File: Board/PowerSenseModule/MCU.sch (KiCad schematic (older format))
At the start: 33 parts, among them J3 Programming Header, J4 Conn_01x02_Male, U2 NCV2007x, U3 dsPIC33EV32GM102, U4 MCP2542FDxMF

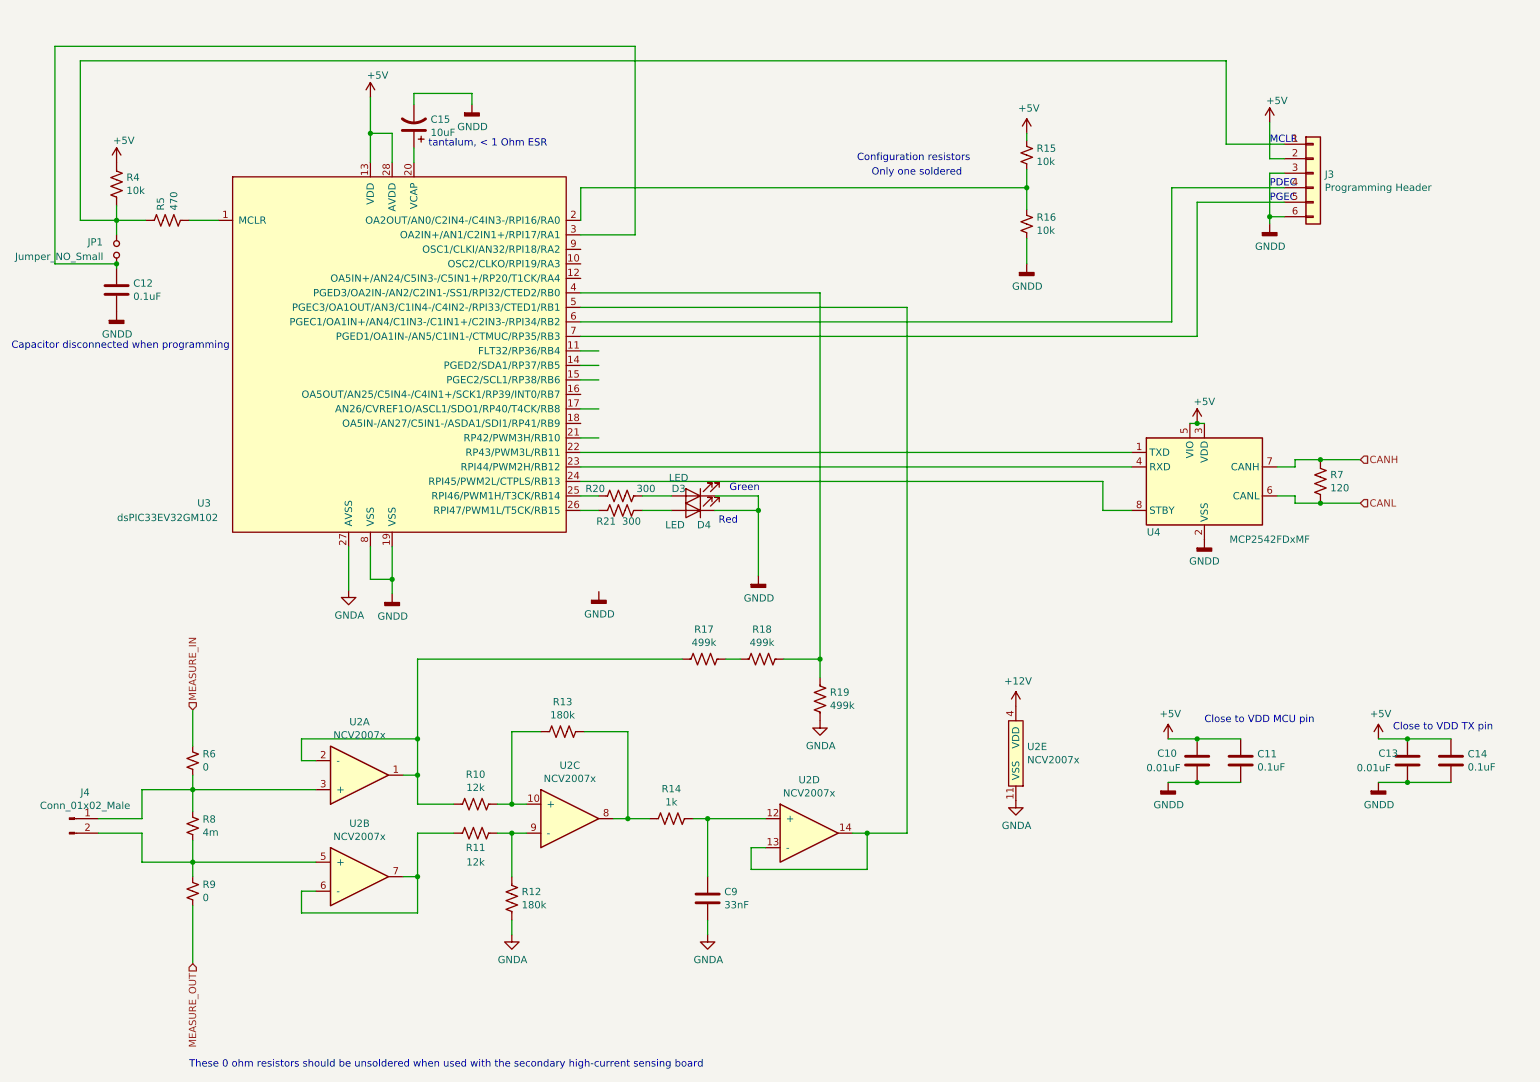
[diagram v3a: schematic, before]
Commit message: FINAL BASIS/REFERENCE
Rewiring done to proper pins on MCU
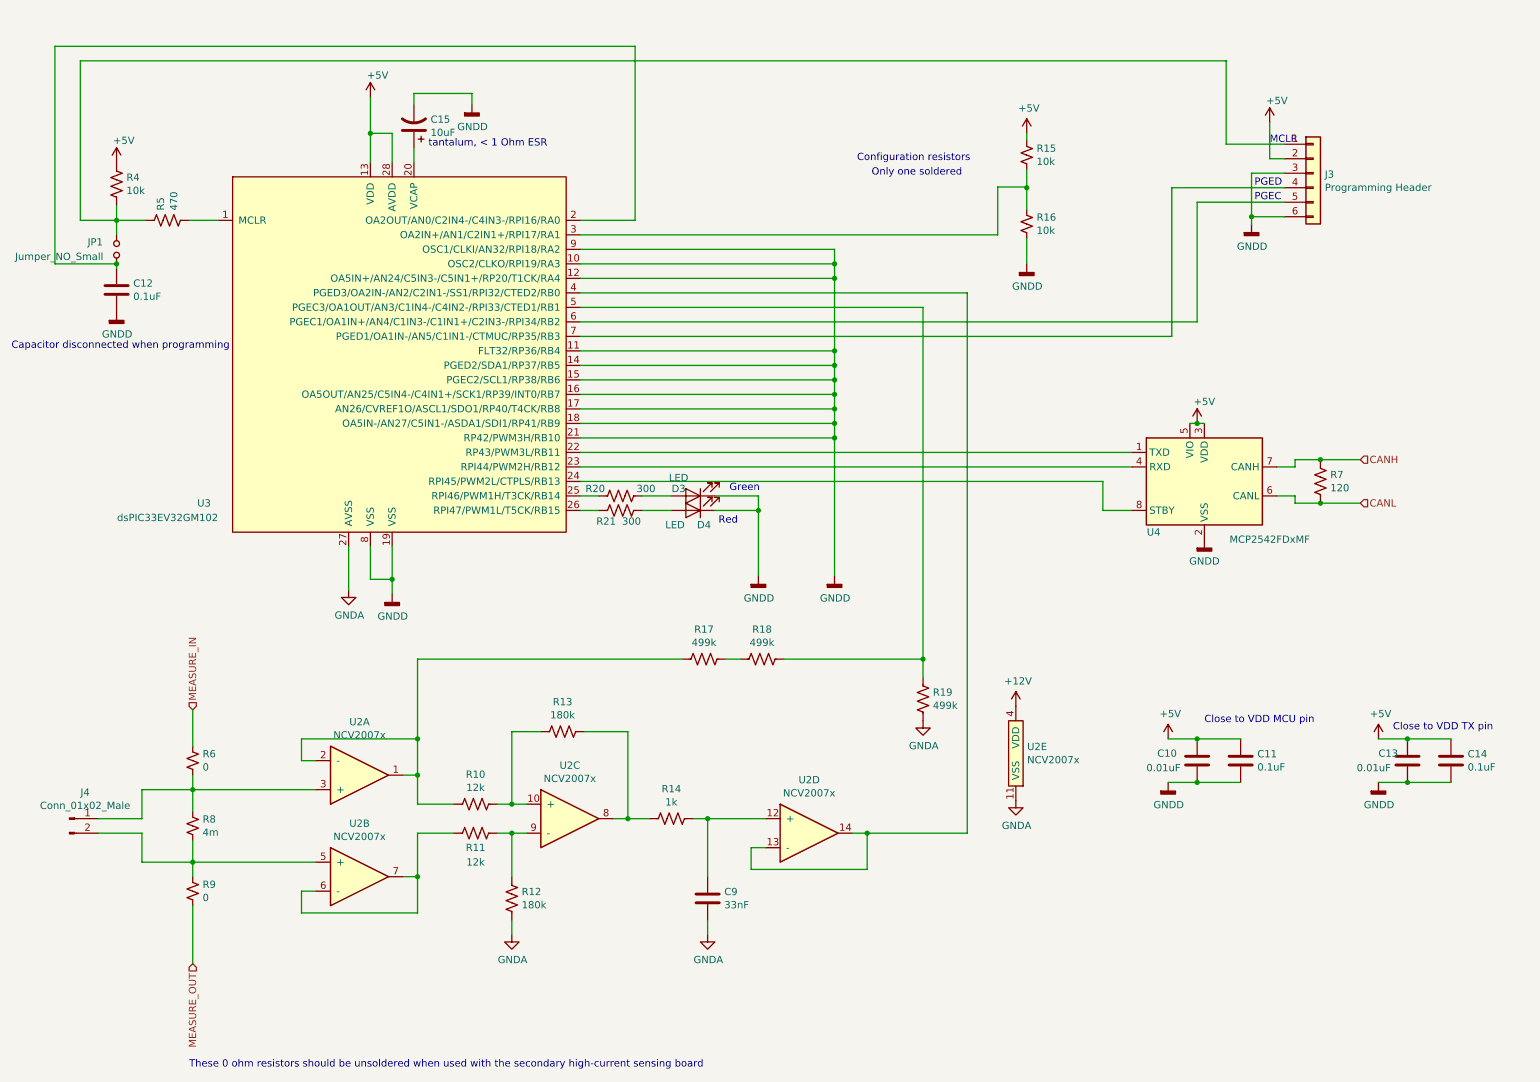
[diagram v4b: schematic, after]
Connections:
- wire segments 143 -> 159
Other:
- note added: "PGED\n"
- note removed: "PDEC"
- moved on the sheet: R19
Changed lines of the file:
@@
 	1925 1900 1725 1900
-$Comp
-L F1_Microchip_MCUs:dsPIC33EV32GM102 U3
-U 1 1 5D3ED3E3
-P 3175 5150
-F 0 "U3" H 1875 6450 50  0000 R CNN
-F 1 "dsPIC33EV32GM102" H 1925 6350 50  0000 R CNN
-F 2 "Package_SO:SSOP-28_5.3x10.2mm_P0.65mm" H 3175 5150 50  0001 C CNN
-F 3 "http://ww1.microchip.com/downloads/en/DeviceDoc/dsPIC33EVXXXGM00X-10X-Family-Data-Sheet-DS70005144H.pdf" H 3175 5150 50  0001 C CNN
-	1    3175 5150
-	1    0    0    -1
-$EndComp
 $Comp
 L Interface_CAN_LIN:MCP2542FDxMF U4
@@
 L power:GNDD #PWR028
 U 1 1 5D3C46D6
-P 9175 1925
-F 0 "#PWR028" H 9175 1675 50  0001 C CNN
-F 1 "GNDD" H 9179 1770 50  0000 C CNN
-F 2 "" H 9175 1925 50  0001 C CNN
-F 3 "" H 9175 1925 50  0001 C CNN
-	1    9175 1925
+P 9050 1925
+F 0 "#PWR028" H 9050 1675 50  0001 C CNN
+F 1 "GNDD" H 9054 1770 50  0000 C CNN
+F 2 "" H 9050 1925 50  0001 C CNN
+F 3 "" H 9050 1925 50  0001 C CNN
+	1    9050 1925
 	1    0    0    -1
 $EndComp
 Text Notes 9175 1375 0    50   ~ 0
 MCLR
-Text Notes 9175 1775 0    50   ~ 0
+Text Notes 9070 1770 0    50   ~ 0
 PGEC
-Text Notes 9175 1675 0    50   ~ 0
-PDEC
+Text Notes 9070 1670 0    50   ~ 0
+PGED\n
 Wire Wire Line
 	8875 1375 9275 1375
@@
 	975  1900 975  800
 Wire Wire Line
-	9175 1875 9175 1925
-Wire Wire Line
-	9275 1875 9175 1875
-Connection ~ 9175 1875
-Wire Wire Line
-	9175 1575 9175 1875
+	9050 1875 9050 1925
+Connection ~ 9050 1875
+Wire Wire Line
+	9050 1575 9050 1875
 Text HLabel 9800 3850 2    50   Input ~ 0
 CANL
@@
 Wire Wire Line
 	975  1900 1225 1900
-Wire Wire Line
-	9275 1575 9175 1575
 Wire Wire Line
 	9175 1475 9175 1225
@@
 Wire Wire Line
 	5300 6825 5300 6725
-Wire Wire Line
-	6400 6125 6675 6125
 Connection ~ 6400 6125
 $Comp
@@
 Wire Wire Line
 	3300 4925 3300 5475
-Connection ~ 6075 4925
 $Comp
 L power:GNDA #PWR0101
 U 1 1 5D62FB9E
-P 6075 5350
-F 0 "#PWR0101" H 6075 5100 50  0001 C CNN
-F 1 "GNDA" H 6080 5177 50  0000 C CNN
-F 2 "" H 6075 5350 50  0001 C CNN
-F 3 "" H 6075 5350 50  0001 C CNN
-	1    6075 5350
+P 6785 5350
+F 0 "#PWR0101" H 6785 5100 50  0001 C CNN
+F 1 "GNDA" H 6790 5177 50  0000 C CNN
+F 2 "" H 6785 5350 50  0001 C CNN
+F 3 "" H 6785 5350 50  0001 C CNN
+	1    6785 5350
 	1    0    0    -1
 $EndComp
@@
 	3300 4925 5125 4925
 Wire Wire Line
-	6075 4925 6075 5050
-Wire Wire Line
-	5825 4925 6075 4925
+	6785 4925 6785 5050
 Wire Wire Line
 	5525 4925 5425 4925
@@
 L Device:R_US R19
 U 1 1 5D60BC64
-P 6075 5200
-F 0 "R19" H 6007 5154 50  0000 R CNN
-F 1 "499k" H 6007 5245 50  0000 R CNN
-F 2 "Resistor_SMD:R_0603_1608Metric_Pad1.05x0.95mm_HandSolder" V 6115 5190 50  0001 C CNN
-F 3 "~" H 6075 5200 50  0001 C CNN
-	1    6075 5200
+P 6785 5200
+F 0 "R19" H 6717 5154 50  0000 R CNN
+F 1 "499k" H 6717 5245 50  0000 R CNN
+F 2 "Resistor_SMD:R_0603_1608Metric_Pad1.05x0.95mm_HandSolder" V 6825 5190 50  0001 C CNN
+F 3 "~" H 6785 5200 50  0001 C CNN
+	1    6785 5200
 	-1   0    0    1
 $EndComp
@@
 L power:GNDD #PWR0105
 U 1 1 5D4D1DB2
-P 4550 4460
-F 0 "#PWR0105" H 4550 4210 50  0001 C CNN
-F 1 "GNDD" H 4554 4305 50  0000 C CNN
-F 2 "" H 4550 4460 50  0001 C CNN
-F 3 "" H 4550 4460 50  0001 C CNN
-	1    4550 4460
-	1    0    0    -1
-$EndComp
-Wire Wire Line
-	4425 2800 4550 2800
-Wire Wire Line
-	4425 2900 4550 2900
-Wire Wire Line
-	4425 3000 4550 3000
-Wire Wire Line
-	4425 3200 4550 3200
-Wire Wire Line
-	4425 3400 4550 3400
+P 6175 4350
+F 0 "#PWR0105" H 6175 4100 50  0001 C CNN
+F 1 "GNDD" H 6179 4195 50  0000 C CNN
+F 2 "" H 6175 4350 50  0001 C CNN
+F 3 "" H 6175 4350 50  0001 C CNN
+	1    6175 4350
+	1    0    0    -1
+$EndComp
 Wire Wire Line
 	4425 3800 4550 3800
@@
 	8875 800  975  800
 Wire Wire Line
-	8500 1675 8500 2600
-Wire Wire Line
-	4425 2600 8500 2600
-Wire Wire Line
-	8675 1775 8675 2700
-Wire Wire Line
-	4425 2700 8675 2700
-Wire Wire Line
-	6075 2400 4425 2400
-Wire Wire Line
-	6075 2400 6075 4925
-Wire Wire Line
-	6675 2500 4425 2500
-Wire Wire Line
-	6675 2500 6675 6125
-Wire Wire Line
-	4800 2000 4425 2000
-Wire Wire Line
-	4800 700  4800 2000
-Wire Wire Line
-	4425 1675 4425 1900
-Wire Wire Line
-	4425 1675 7500 1675
+	6785 4925 6785 2500
+Connection ~ 6785 4925
+Wire Wire Line
+	8675 1775 8675 2600
+Wire Wire Line
+	4425 2600 8675 2600
+Wire Wire Line
+	8500 1675 8500 2700
+Wire Wire Line
+	8500 2700 4425 2700
+Wire Wire Line
+	9050 1875 9275 1875
+Wire Wire Line
+	9050 1575 9275 1575
+$Comp
+L F1_Microchip_MCUs:dsPIC33EV32GM102 U3
+U 1 1 5D3ED3E3
+P 3175 5150
+F 0 "U3" H 1875 6450 50  0000 R CNN
+F 1 "dsPIC33EV32GM102" H 1925 6350 50  0000 R CNN
+F 2 "Package_SO:SSOP-28_5.3x10.2mm_P0.65mm" H 3175 5150 50  0001 C CNN
+F 3 "http://ww1.microchip.com/downloads/en/DeviceDoc/dsPIC33EVXXXGM00X-10X-Family-Data-Sheet-DS70005144H.pdf" H 3175 5150 50  0001 C CNN
+	1    3175 5150
+	1    0    0    -1
+$EndComp
+Wire Wire Line
+	7500 1670 7300 1670
+Wire Wire Line
+	7300 1670 7300 2000
+Wire Wire Line
+	4425 2000 7300 2000
+Wire Wire Line
+	4800 700  4800 1900
+Wire Wire Line
+	4800 1900 4425 1900
+Wire Wire Line
+	6400 6125 7090 6125
+Wire Wire Line
+	7090 6125 7090 2400
+Wire Wire Line
+	7090 2400 4425 2400
+Wire Wire Line
+	5825 4925 6785 4925
+Wire Wire Line
+	4425 2500 6785 2500
+Wire Wire Line
+	4425 2800 6175 2800
+Wire Wire Line
+	4425 2900 6175 2900
+Connection ~ 6175 2900
+Wire Wire Line
+	6175 2900 6175 3000
+Wire Wire Line
+	4425 3000 6175 3000
+Connection ~ 6175 3000
+Wire Wire Line
+	6175 3000 6175 3100
+Wire Wire Line
+	4425 3100 6175 3100
+Connection ~ 6175 3100
+Wire Wire Line
+	4425 3200 6175 3200
+Wire Wire Line
+	6175 3100 6175 3200
+Connection ~ 6175 3200
+Wire Wire Line
+	6175 3200 6175 3300
+Wire Wire Line
+	4425 3400 6175 3400
+Connection ~ 6175 3400
+Wire Wire Line
+	6175 3400 6175 4350
+Wire Wire Line
+	4425 3300 6175 3300
+Connection ~ 6175 3300
+Wire Wire Line
+	6175 3300 6175 3400
+Wire Wire Line
+	4425 2100 6175 2100
+Connection ~ 6175 2800
+Wire Wire Line
+	6175 2800 6175 2900
+Wire Wire Line
+	4425 2200 6175 2200
+Wire Wire Line
+	6175 2100 6175 2200
+Connection ~ 6175 2200
+Wire Wire Line
+	6175 2200 6175 2300
+Wire Wire Line
+	4425 2300 6175 2300
+Connection ~ 6175 2300
+Wire Wire Line
+	6175 2300 6175 2800
 $EndSCHEMATC

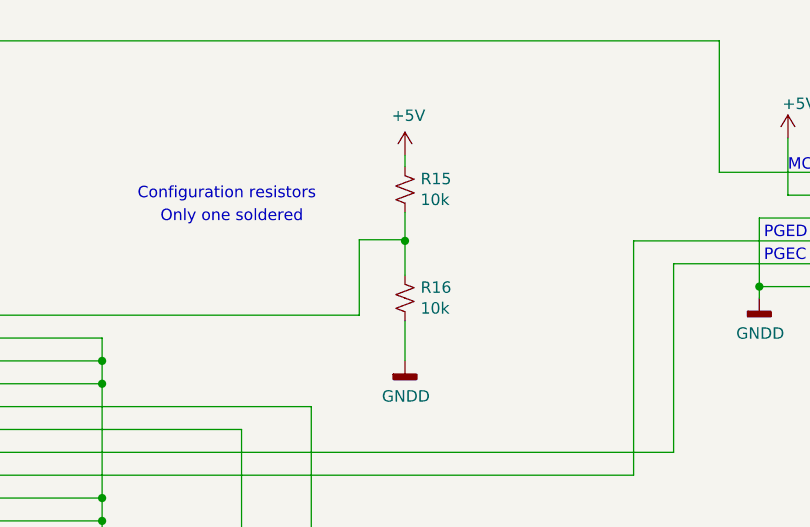
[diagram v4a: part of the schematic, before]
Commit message: Redesign/Configuration Resistors Fixed
Dimensions for PCB defined, might need to be extended for mounting. Rewiring being done to fit dimensions.
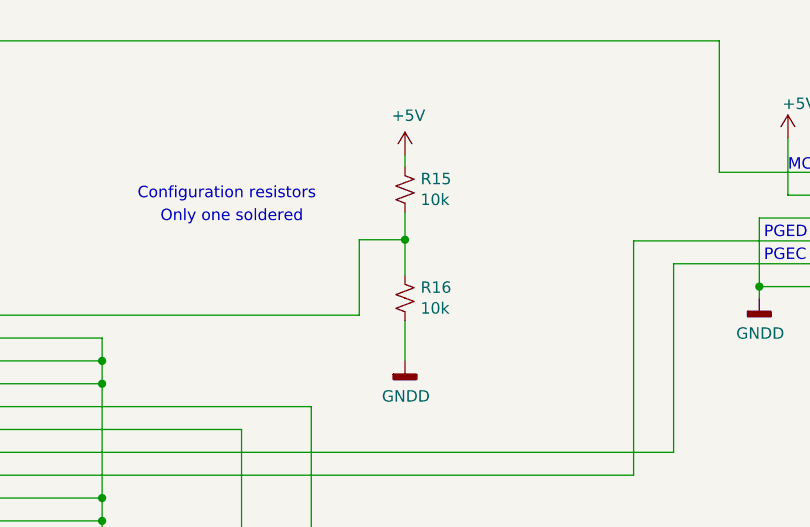
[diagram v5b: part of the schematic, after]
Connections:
- net at U3.3 (OA2IN+/AN1/C2IN1+/RPI17/RA1): now also R15.2, R16.1
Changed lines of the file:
@@
 Wire Wire Line
 	3675 1025 3675 1100
-Wire Wire Line
-	7500 1550 7500 1675
-Connection ~ 7500 1675
-Wire Wire Line
-	7500 1675 7500 1825
 Connection ~ 3300 5475
 Wire Wire Line
@@
 $EndComp
 Wire Wire Line
-	7495 1675 7495 1670
-Wire Wire Line
-	7500 1675 7495 1675
-Wire Wire Line
 	4425 3600 8225 3600
 Wire Wire Line
@@
 Wire Wire Line
 	6175 2300 6175 2800
+Wire Wire Line
+	7500 1670 7500 1550
+Wire Wire Line
+	7500 1670 7500 1825
+Connection ~ 7500 1670
 $EndSCHEMATC

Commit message: OP amp circuit changes
Move D op amp to voltage sensing 
Changed voltage divider resistors to smaller values
Changed error in differential amp resistor values (gain)
Changed error in resistors have capacitor footprints
Added datasheet link for the op amps
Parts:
- added C16: 33nF, Capacitor_SMD:C_0603_1608Metric_Pad1.05x0.95mm_HandSolder, symbol Device:C
- added R22: 1k, Resistor_SMD:R_0603_1608Metric_Pad1.05x0.95mm_HandSolder, symbol Device:R_US
- R10, R11: value 12k -> 1.2k; footprint Capacitor_SMD:C_0603_1608Metric_Pad1.05x0.95mm_HandSolder -> Resistor_SMD:R_0603_1608Metric_Pad1.05x0.95mm_HandSolder
- R12, R13: value 180k -> 75k; footprint Capacitor_SMD:C_0603_1608Metric_Pad1.05x0.95mm_HandSolder -> Resistor_SMD:R_0603_1608Metric_Pad1.05x0.95mm_HandSolder
- R14, R15, R16, R9: footprint Capacitor_SMD:C_0603_1608Metric_Pad1.05x0.95mm_HandSolder -> Resistor_SMD:R_0603_1608Metric_Pad1.05x0.95mm_HandSolder
- R17, R19: value 499k -> 4.99k
- R18: value 499k -> 10k
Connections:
- net GNDA: now also C16.2
- net at U2.13 (-), U2.14: now also R22.2; no longer U3.4 (PGED3/OA2IN-/AN2/C2IN1-/SS1/RPI32/CTED2/RB0)
- net at R18.1, R19.2: now also U2.12 (+); no longer U3.5 (PGEC3/OA1OUT/AN3/C1IN4-/C4IN2-/RPI33/CTED1/RB1)
- net at R10.1, R13.2: now also U2.9 (-); no longer U2.10 (+)
- net at R11.1, R12.1: now also U2.10 (+); no longer U2.9 (-)
- net at C9.1, R14.1: now also U3.4 (PGED3/OA2IN-/AN2/C2IN1-/SS1/RPI32/CTED2/RB0); no longer U2.12 (+)
- new net: C16.1, R22.1, U3.5 (PGEC3/OA1OUT/AN3/C1IN4-/C4IN2-/RPI33/CTED1/RB1)
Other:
- moved on the sheet: R17, R18, R19, U2D

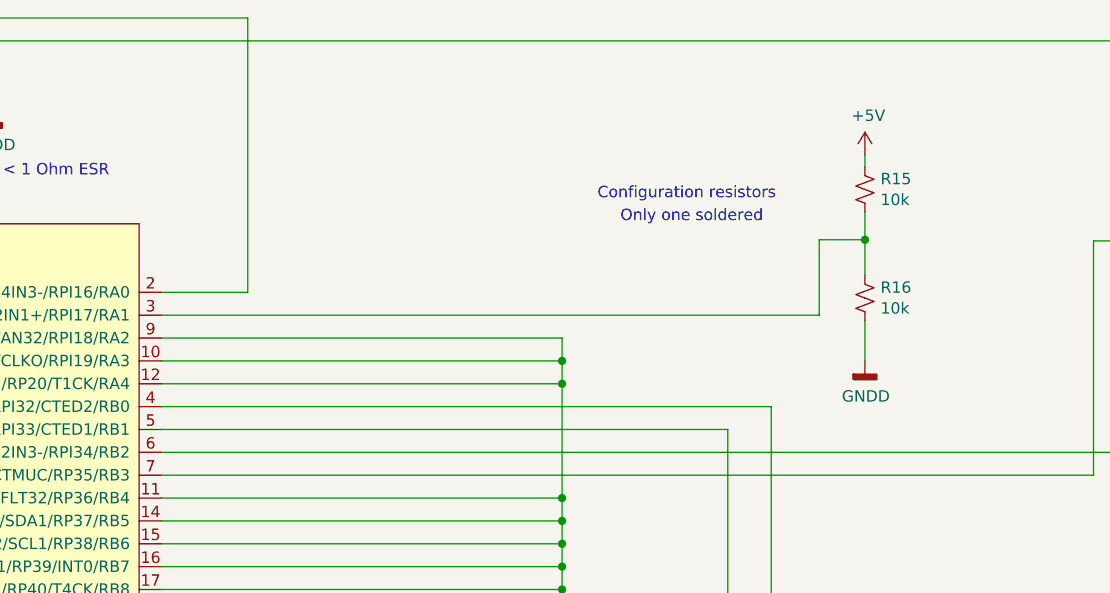
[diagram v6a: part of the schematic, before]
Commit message: Every component wired.
Each component is wired. I've now decided to make this PCB symmetric though.
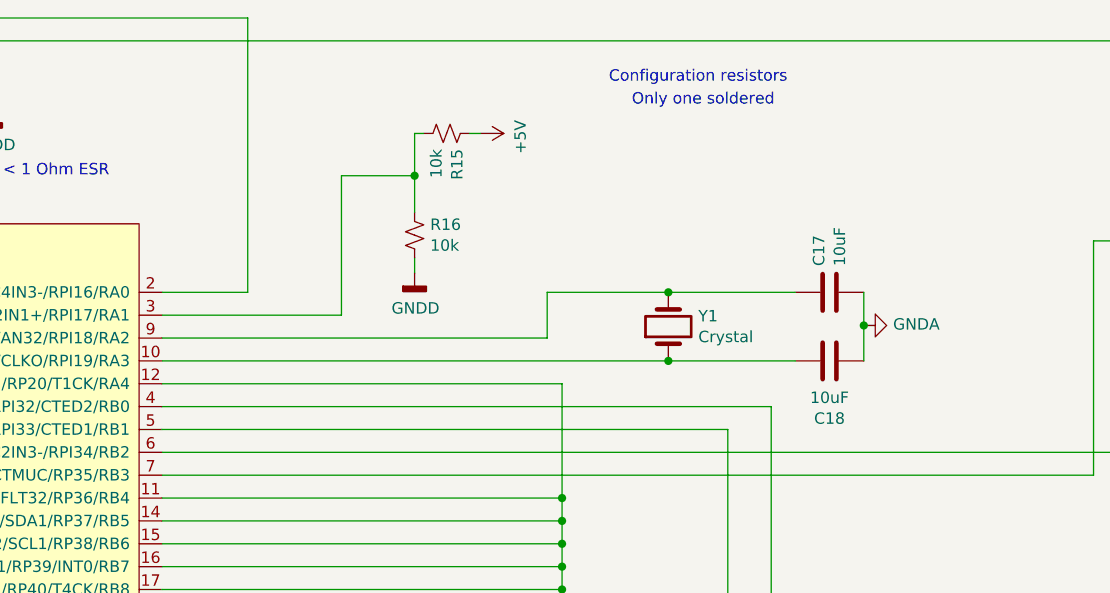
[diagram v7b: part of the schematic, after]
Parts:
- added C17, C18: 10uF, Capacitor_SMD:C_0603_1608Metric_Pad1.05x0.95mm_HandSolder, symbol Device:C
- added Y1: Crystal, Crystal_SMD_2520-4Pin_2.5x2.0mm.kicad_mod_IEEE.kicad_mod, symbol Device:Crystal
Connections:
- net GNDA: now also C17.2, C18.2
- net GNDD: no longer U3.10 (OSC2/CLKO/RPI19/RA3), U3.9 (OSC1/CLKI/AN32/RPI18/RA2)
- new net: C18.1, U3.10 (OSC2/CLKO/RPI19/RA3), Y1.1
- new net: C17.1, U3.9 (OSC1/CLKI/AN32/RPI18/RA2), Y1.2
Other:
- moved on the sheet: R15, R16
